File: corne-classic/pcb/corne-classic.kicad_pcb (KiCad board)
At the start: 2 copper layers, 133.8 x 92.2 mm, 98 parts, among them J1 MJ-4PP-9, J2 OLED, J3 LED, P1 i2c-pin, P2 i2c-pin, SW1 SW_PUSH, SW10 SW_PUSH, SW11 SW_PUSH, SW12 SW_PUSH, SW13 SW_PUSH, SW14 SW_PUSH, SW15 SW_PUSH, SW16 SW_PUSH, SW17 SW_PUSH, SW18 SW_PUSH, SW19 SW_PUSH, SW2 SW_PUSH, SW20 SW_PUSH, SW21 SW_PUSH, SW3 SW_PUSH, SW4 SW_PUSH, SW5 SW_PUSH, SW6 SW_PUSH, SW7 SW_PUSH, SW8 SW_PUSH, SW9 SW_PUSH, U1 ProMicro

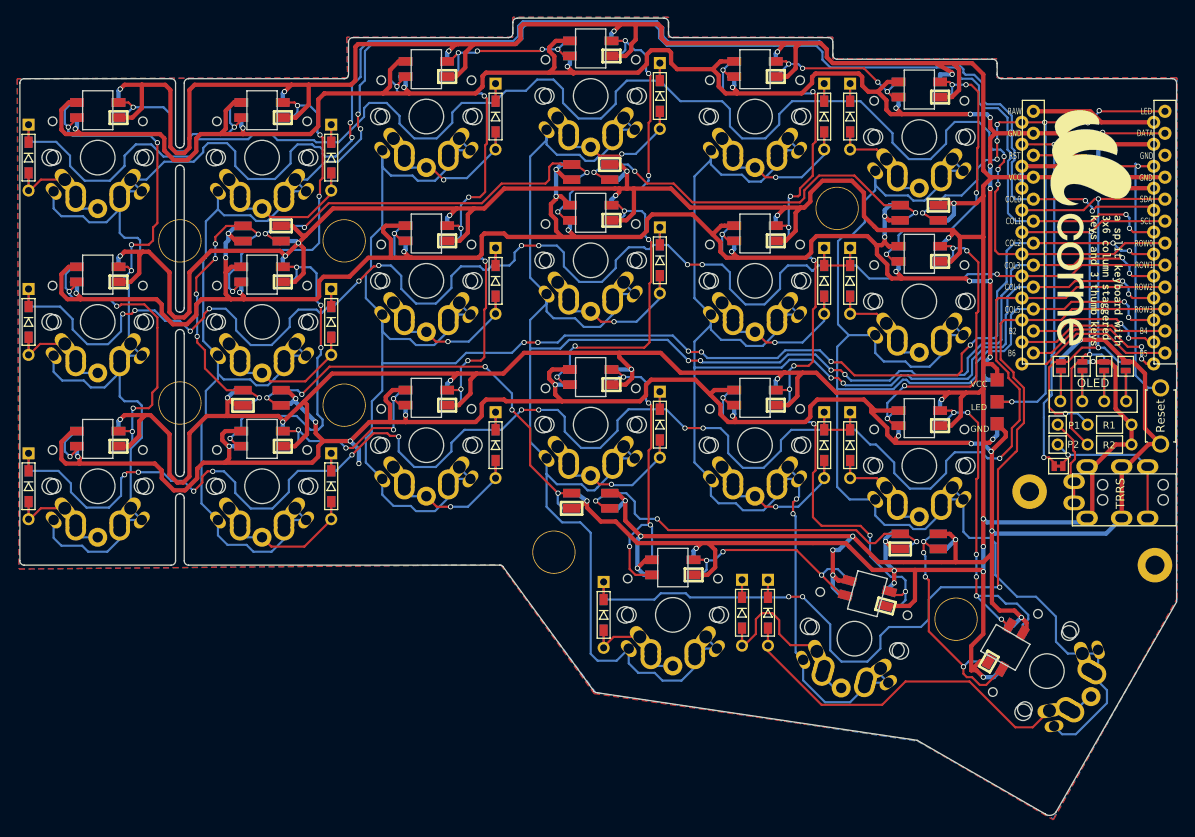
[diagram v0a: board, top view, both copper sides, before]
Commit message: remove snap offs and holes
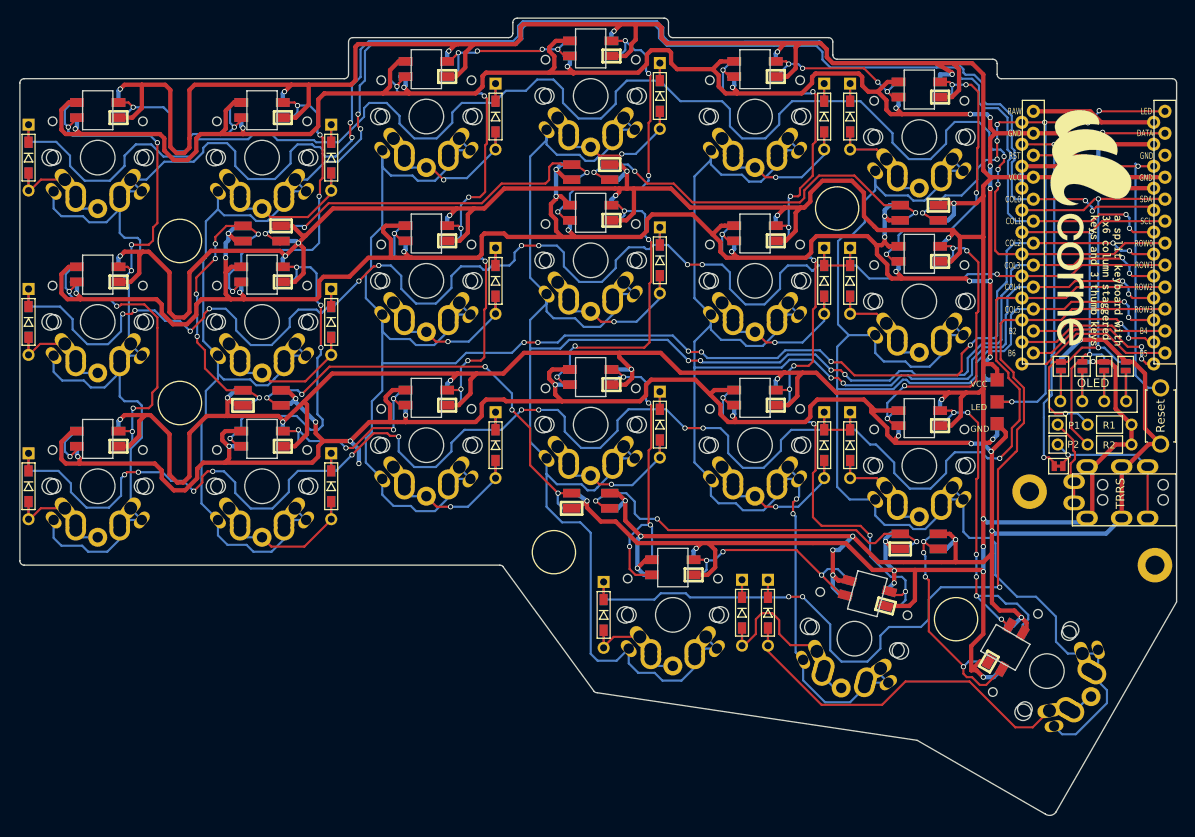
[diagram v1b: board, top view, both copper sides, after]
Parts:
- removed the ? at (79.5, 105.5)
- removed the ? at (79.5, 86.8)
- removed the ? at (98.5, 86.8)
- removed the ? at (98.5, 105.8)
- removed the ? at (155.5, 83.0)
- removed the ? at (122.8, 122.8)
- removed the ? at (169.2, 130.5)
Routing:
- removed copper zone on B.Cu, net GND
- removed copper zone on F.Cu, net GND
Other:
- outline, holes or cut-outs redrawn
